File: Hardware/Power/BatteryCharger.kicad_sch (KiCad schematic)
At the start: 18 parts, among them Q9 Si7141DP, U6 LTC4002ES8-8.4

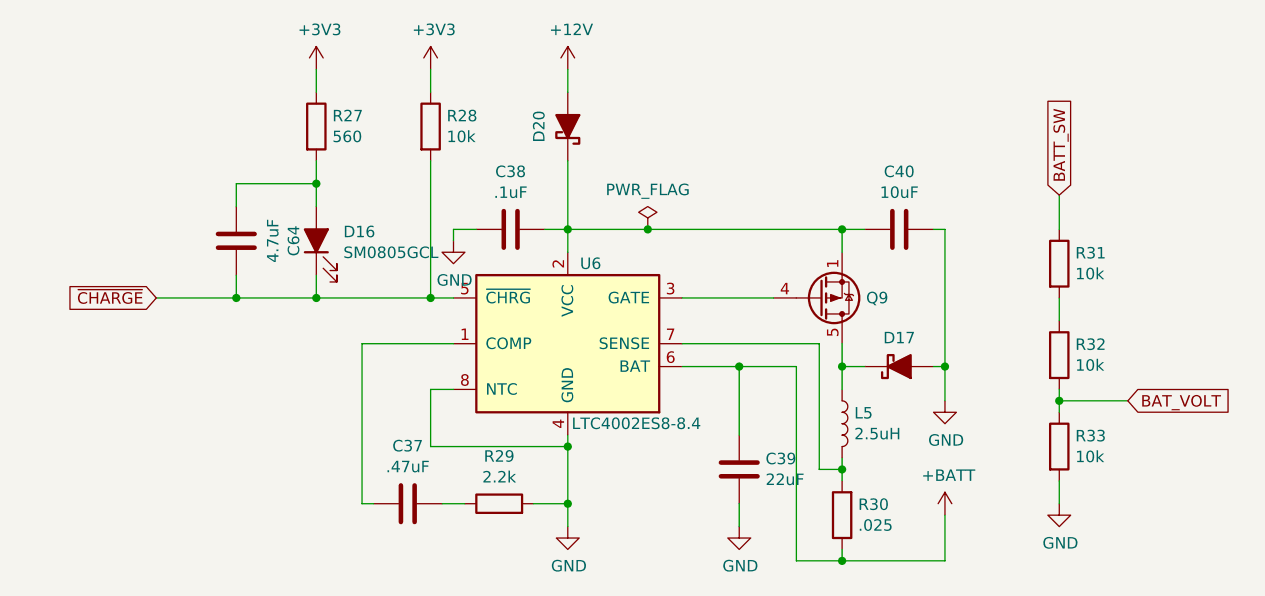
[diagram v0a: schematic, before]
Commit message: Update to kicad 8
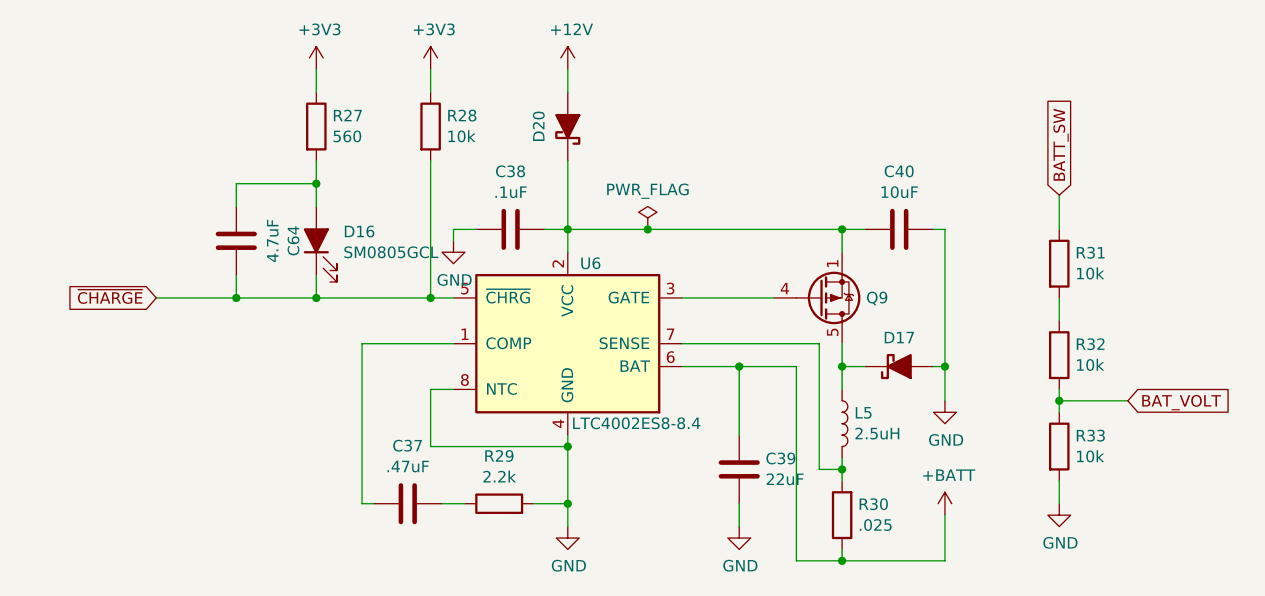
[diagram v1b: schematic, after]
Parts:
- D16: footprint LED_SMD:LED_0805_2012Metric_Castellated -> LED_SMD:LED_0805_2012Metric
